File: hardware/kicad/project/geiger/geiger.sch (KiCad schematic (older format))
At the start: 41 parts, among them J1 Pulse Out, J2 I2C OLED 128x64 with SH1106, Q1 BC328, Q2 MPSA44, Q3 BC517, U1 EzSBC_ESP32-01, U2 TLC555xP, U3 TLC555xP

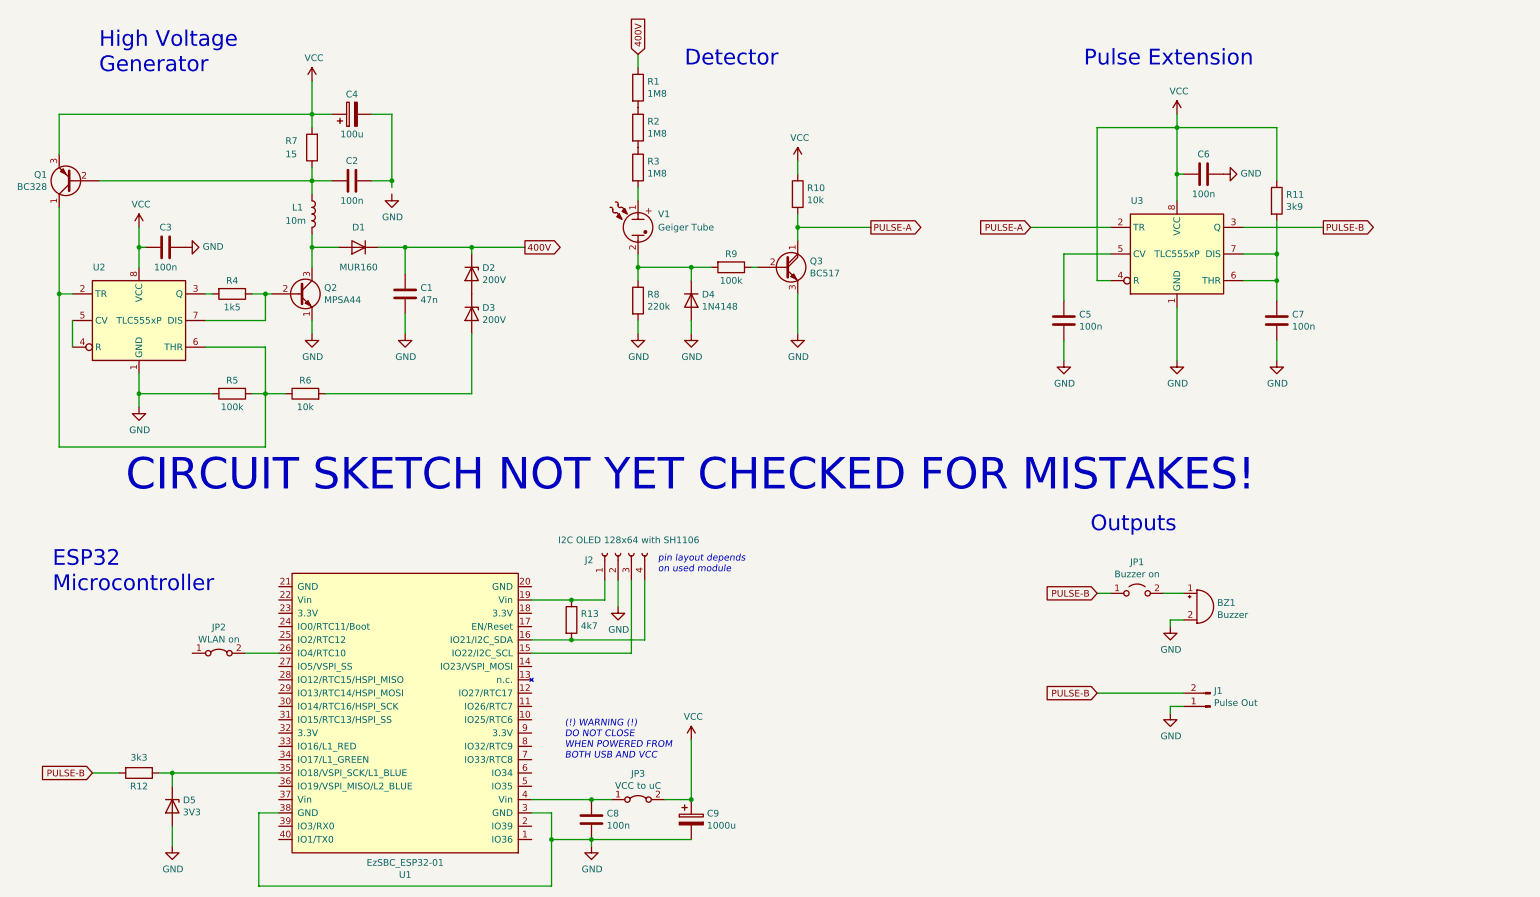
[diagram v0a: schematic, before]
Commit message: checked and corrected KiCad schematic
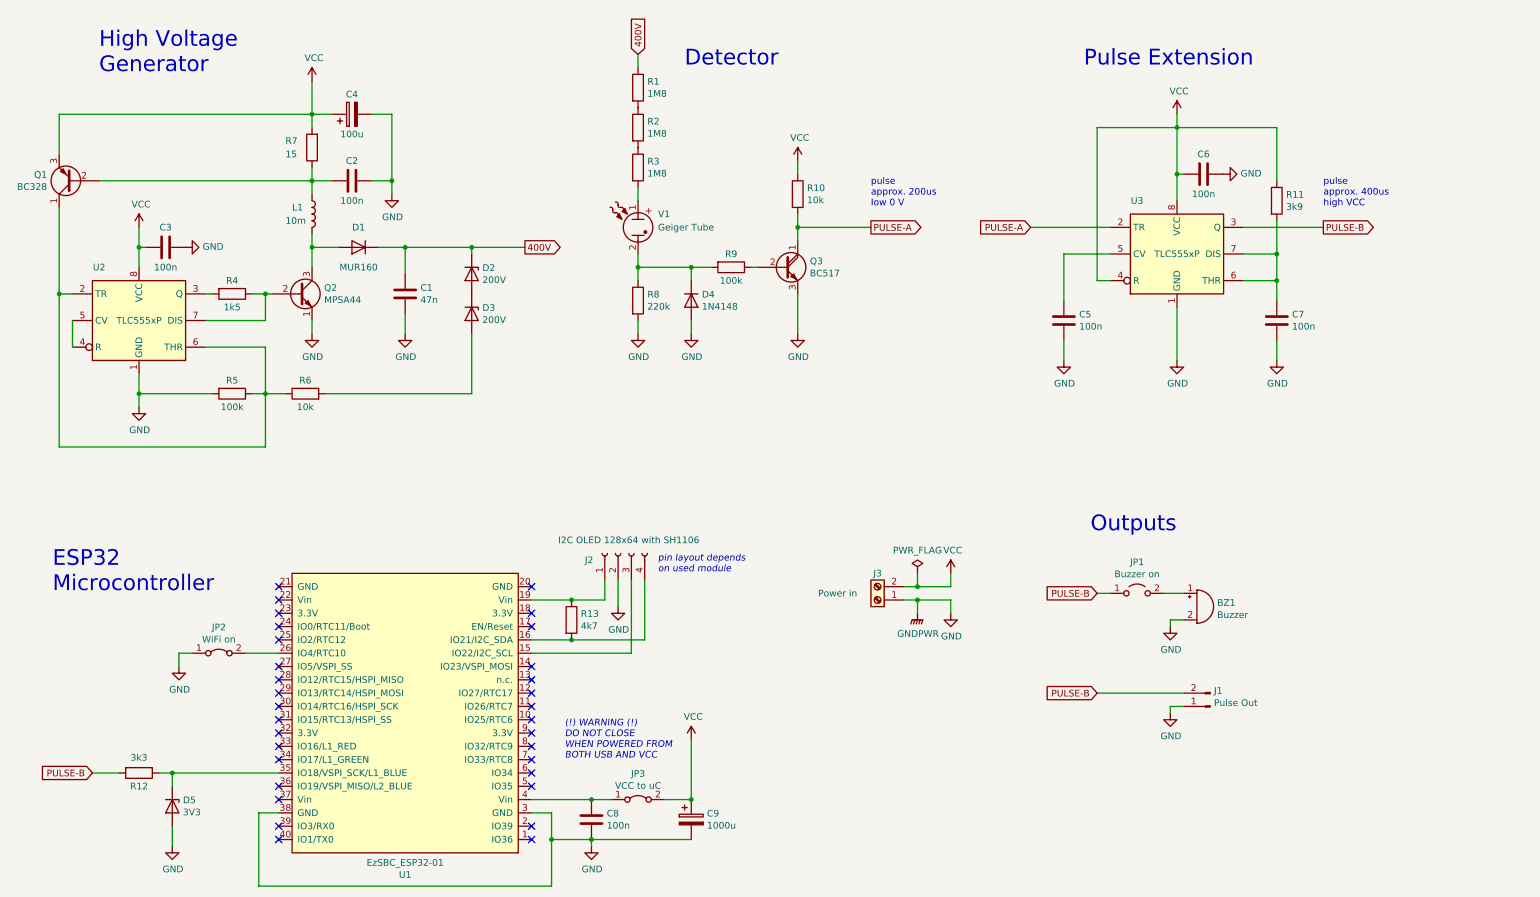
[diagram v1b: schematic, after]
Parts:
- added J3: Power in, symbol Connector:Screw_Terminal_01x02
- JP2: value WLAN on -> WiFi on
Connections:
- net GND: now also C2.1, C4.2, JP2.1 (A), J3.1 (Pin_1)
- net VCC: now also J3.2 (Pin_2)
- no-connect marks 0 -> 32
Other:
- note added: "pulse\napprox. 200us\nlow 0 V"
- note added: "pulse\napprox. 400us\nhigh VCC"
- note removed: "CIRCUIT SKETCH NOT YET CHECKED FOR MISTAKES!"
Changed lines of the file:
@@
 Sheet 1 1
 Title "ESP32 Geiger Counter"
-Date "2021-01-29"
+Date "2021-01-30"
 Rev ""
 Comp "Holger Fleischmann"
@@
 	2950 1750 2950 1650
 Wire Wire Line
-	2950 1650 1050 1650
-Wire Wire Line
 	1050 1650 1050 1950
 Wire Wire Line
@@
 	3100 1650 2950 1650
 Wire Wire Line
-	3550 2150 3550 2200
-Wire Wire Line
 	3400 2150 3550 2150
 Wire Wire Line
@@
 Wire Wire Line
 	2700 5700 2450 5700
-$Comp
-L Jumper:Jumper_2_Bridged JP2
-U 1 1 60343981
-P 2250 5700
-F 0 "JP2" H 2250 5895 50  0000 C CNN
-F 1 "WLAN on" H 2250 5804 50  0000 C CNN
-F 2 "" H 2250 5700 50  0001 C CNN
-F 3 "~" H 2250 5700 50  0001 C CNN
-	1    2250 5700
-	1    0    0    -1
-$EndComp
 Wire Wire Line
 	5050 6800 5200 6800
@@
 Wire Wire Line
 	4900 5600 5450 5600
-Text Notes 1550 4500 0    236  ~ 0
-CIRCUIT SKETCH NOT YET CHECKED FOR MISTAKES!
+Text Notes 7150 2350 0    50   ~ 0
+pulse\napprox. 200us\nlow 0 V
+Text Notes 10550 2350 0    50   ~ 0
+pulse\napprox. 400us\nhigh VCC
+Wire Wire Line
+	3550 2150 3550 2250
+NoConn ~ 2700 5200
+NoConn ~ 2700 5300
+NoConn ~ 2700 5400
+NoConn ~ 2700 5500
+NoConn ~ 2700 5600
+NoConn ~ 2700 5800
+NoConn ~ 2700 5900
+NoConn ~ 2700 6000
+NoConn ~ 2700 6100
+NoConn ~ 2700 6200
+NoConn ~ 2700 6300
+NoConn ~ 2700 6400
+NoConn ~ 2700 6500
+NoConn ~ 2700 6700
+NoConn ~ 2700 6800
+NoConn ~ 4600 5200
+NoConn ~ 4600 5400
+NoConn ~ 4600 5500
+NoConn ~ 4600 5800
+NoConn ~ 4600 5900
+NoConn ~ 4600 6000
+NoConn ~ 4600 6100
+NoConn ~ 4600 6200
+NoConn ~ 4600 6300
+NoConn ~ 4600 6400
+NoConn ~ 4600 6500
+NoConn ~ 4600 6600
+NoConn ~ 4600 6700
+NoConn ~ 4600 7000
+NoConn ~ 2700 7000
+NoConn ~ 2700 7100
+NoConn ~ 4600 7100
+$Comp
+L power:GND #PWR0101
+U 1 1 601D64A6
+P 1950 5800
+F 0 "#PWR0101" H 1950 5550 50  0001 C CNN
+F 1 "GND" H 1955 5627 50  0000 C CNN
+F 2 "" H 1950 5800 50  0001 C CNN
+F 3 "" H 1950 5800 50  0001 C CNN
+	1    1950 5800
+	1    0    0    -1
+$EndComp
+Wire Wire Line
+	2050 5700 1950 5700
+Wire Wire Line
+	1950 5700 1950 5800
+$Comp
+L Jumper:Jumper_2_Bridged JP2
+U 1 1 60343981
+P 2250 5700
+F 0 "JP2" H 2250 5895 50  0000 C CNN
+F 1 "WiFi on" H 2250 5804 50  0000 C CNN
+F 2 "" H 2250 5700 50  0001 C CNN
+F 3 "~" H 2250 5700 50  0001 C CNN
+	1    2250 5700
+	1    0    0    -1
+$EndComp
+Wire Wire Line
+	1050 1650 2950 1650
+$Comp
+L power:GND #PWR024
+U 1 1 601E1EB9
+P 7750 5400
+F 0 "#PWR024" H 7750 5150 50  0001 C CNN
+F 1 "GND" H 7755 5227 50  0000 C CNN
+F 2 "" H 7750 5400 50  0001 C CNN
+F 3 "" H 7750 5400 50  0001 C CNN
+	1    7750 5400
+	1    0    0    -1
+$EndComp
+$Comp
+L power:VCC #PWR023
+U 1 1 601E23DB
+P 7750 5100
+F 0 "#PWR023" H 7750 4950 50  0001 C CNN
+F 1 "VCC" H 7765 5273 50  0000 C CNN
+F 2 "" H 7750 5100 50  0001 C CNN
+F 3 "" H 7750 5100 50  0001 C CNN
+	1    7750 5100
+	1    0    0    -1
+$EndComp
+$Comp
+L Connector:Screw_Terminal_01x02 J3
+U 1 1 601E2CC3
+P 7200 5300
+F 0 "J3" H 7200 5100 50  0000 C CNN
+F 1 "Power in" H 7500 5250 50  0000 C CNN
+F 2 "" H 7200 5300 50  0001 C CNN
+F 3 "~" H 7200 5300 50  0001 C CNN
+	1    7200 5300
+	-1   0    0    1
+$EndComp
+Wire Wire Line
+	7400 5300 7500 5300
+$Comp
+L power:GNDPWR #PWR0102
+U 1 1 601FD717
+P 7500 5400
+F 0 "#PWR0102" H 7500 5200 50  0001 C CNN
+F 1 "GNDPWR" H 7504 5246 50  0000 C CNN
+F 2 "" H 7500 5350 50  0001 C CNN
+F 3 "" H 7500 5350 50  0001 C CNN
+	1    7500 5400
+	1    0    0    -1
+$EndComp
+$Comp
+L power:PWR_FLAG #FLG0101
+U 1 1 601FEC15
+P 7500 5100
+F 0 "#FLG0101" H 7500 5175 50  0001 C CNN
+F 1 "PWR_FLAG" H 7500 5273 50  0000 C CNN
+F 2 "" H 7500 5100 50  0001 C CNN
+F 3 "~" H 7500 5100 50  0001 C CNN
+	1    7500 5100
+	1    0    0    -1
+$EndComp
+Wire Wire Line
+	7500 5400 7500 5300
+Connection ~ 7500 5300
+Wire Wire Line
+	7400 5200 7500 5200
+Wire Wire Line
+	7500 5100 7500 5200
+Connection ~ 7500 5200
+Wire Wire Line
+	7750 5200 7750 5100
+Wire Wire Line
+	7500 5200 7750 5200
+Wire Wire Line
+	7750 5300 7750 5400
+Wire Wire Line
+	7500 5300 7750 5300
 $EndSCHEMATC

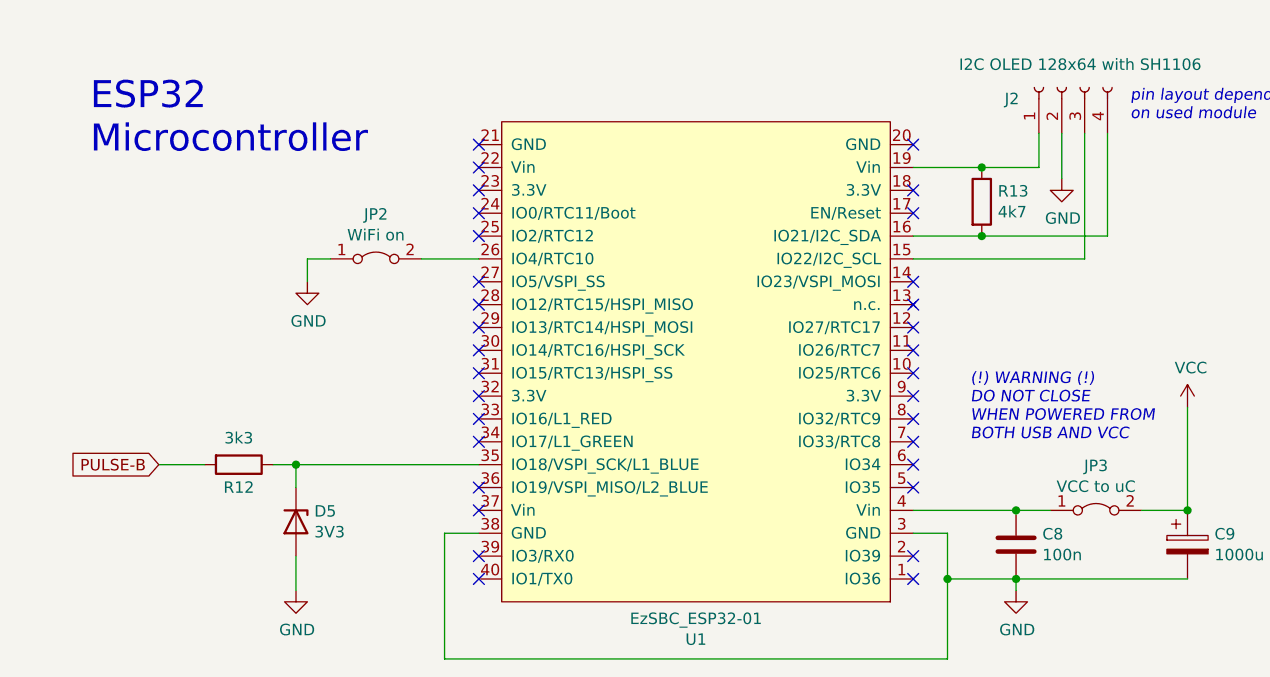
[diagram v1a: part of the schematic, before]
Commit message: changed pins for EZSCB ESP32
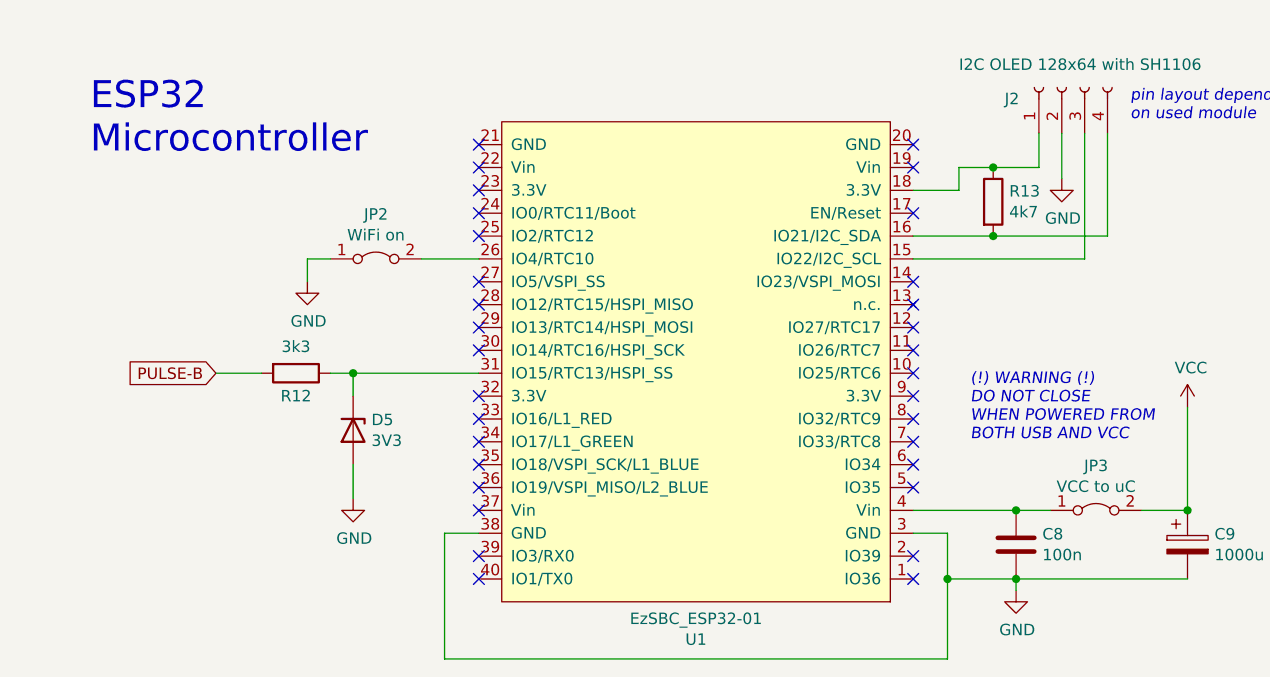
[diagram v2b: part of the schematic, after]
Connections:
- net at D5.1 (K), R12.1: now also U1.31 (IO15/RTC13/HSPI_SS); no longer U1.35 (IO18/VSPI_SCK/L1_BLUE)
- net at U1.18 (3.3V): now also J2.1 (Pin_1), R13.1
- now unconnected: U1.19 (Vin)
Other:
- moved on the sheet: D5, R12, R13
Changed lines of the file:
@@
 Sheet 1 1
 Title "ESP32 Geiger Counter"
-Date "2021-01-30"
+Date "2021-03-07"
 Rev ""
 Comp "Holger Fleischmann"
@@
 L Device:R R12
 U 1 1 602C68B9
-P 1650 6600
-F 0 "R12" V 1750 6600 50  0000 C CNN
-F 1 "3k3" V 1534 6600 50  0000 C CNN
-F 2 "" V 1580 6600 50  0001 C CNN
-F 3 "~" H 1650 6600 50  0001 C CNN
-	1    1650 6600
+P 1900 6200
+F 0 "R12" V 2000 6200 50  0000 C CNN
+F 1 "3k3" V 1784 6200 50  0000 C CNN
+F 2 "" V 1830 6200 50  0001 C CNN
+F 3 "~" H 1900 6200 50  0001 C CNN
+	1    1900 6200
 	0    1    1    0
 $EndComp
@@
 L Device:D_Zener D5
 U 1 1 602C754E
-P 1900 6850
-F 0 "D5" V 1854 6930 50  0000 L CNN
-F 1 "3V3" V 1945 6930 50  0000 L CNN
-F 2 "" H 1900 6850 50  0001 C CNN
-F 3 "~" H 1900 6850 50  0001 C CNN
-	1    1900 6850
+P 2150 6450
+F 0 "D5" V 2104 6530 50  0000 L CNN
+F 1 "3V3" V 2195 6530 50  0000 L CNN
+F 2 "" H 2150 6450 50  0001 C CNN
+F 3 "~" H 2150 6450 50  0001 C CNN
+	1    2150 6450
 	0    1    1    0
 $EndComp
-Text GLabel 1300 6600 0    50   Input ~ 0
+Text GLabel 1550 6200 0    50   Input ~ 0
 PULSE-B
 Wire Wire Line
-	1300 6600 1500 6600
+	1550 6200 1750 6200
 $Comp
 L power:GND #PWR017
 U 1 1 602CD14A
-P 1900 7150
-F 0 "#PWR017" H 1900 6900 50  0001 C CNN
-F 1 "GND" H 1905 6977 50  0000 C CNN
-F 2 "" H 1900 7150 50  0001 C CNN
-F 3 "" H 1900 7150 50  0001 C CNN
-	1    1900 7150
+P 2150 6750
+F 0 "#PWR017" H 2150 6500 50  0001 C CNN
+F 1 "GND" H 2155 6577 50  0000 C CNN
+F 2 "" H 2150 6750 50  0001 C CNN
+F 3 "" H 2150 6750 50  0001 C CNN
+	1    2150 6750
 	1    0    0    -1
 $EndComp
@@
 $EndComp
 Wire Wire Line
-	1800 6600 1900 6600
-Connection ~ 1900 6600
-Wire Wire Line
-	1900 6600 2700 6600
-Wire Wire Line
-	1900 6600 1900 6700
-Wire Wire Line
-	1900 7000 1900 7150
+	2050 6200 2150 6200
+Wire Wire Line
+	2150 6200 2150 6300
+Wire Wire Line
+	2150 6600 2150 6750
 $Comp
 L Device:C C8
@@
 L Device:R R13
 U 1 1 603B2486
-P 4900 5450
-F 0 "R13" H 4970 5496 50  0000 L CNN
-F 1 "4k7" H 4970 5405 50  0000 L CNN
-F 2 "" V 4830 5450 50  0001 C CNN
-F 3 "~" H 4900 5450 50  0001 C CNN
-	1    4900 5450
-	1    0    0    -1
-$EndComp
-Wire Wire Line
-	4600 5600 4900 5600
-Wire Wire Line
-	4600 5300 4900 5300
-Connection ~ 4900 5300
-Wire Wire Line
-	4900 5300 5150 5300
-Connection ~ 4900 5600
-Wire Wire Line
-	4900 5600 5450 5600
+P 4950 5450
+F 0 "R13" H 5020 5496 50  0000 L CNN
+F 1 "4k7" H 5020 5405 50  0000 L CNN
+F 2 "" V 4880 5450 50  0001 C CNN
+F 3 "~" H 4950 5450 50  0001 C CNN
+	1    4950 5450
+	1    0    0    -1
+$EndComp
+Wire Wire Line
+	4600 5600 4950 5600
+Wire Wire Line
+	4950 5300 5150 5300
+Connection ~ 4950 5600
+Wire Wire Line
+	4950 5600 5450 5600
 Text Notes 7150 2350 0    50   ~ 0
 pulse\napprox. 200us\nlow 0 V
@@
 NoConn ~ 2700 6000
 NoConn ~ 2700 6100
-NoConn ~ 2700 6200
 NoConn ~ 2700 6300
 NoConn ~ 2700 6400
@@
 NoConn ~ 2700 6800
 NoConn ~ 4600 5200
-NoConn ~ 4600 5400
 NoConn ~ 4600 5500
 NoConn ~ 4600 5800
@@
 Wire Wire Line
 	7500 5300 7750 5300
+Wire Wire Line
+	4800 5400 4600 5400
+Wire Wire Line
+	4800 5300 4800 5400
+Wire Wire Line
+	4950 5300 4800 5300
+Connection ~ 4950 5300
+NoConn ~ 4600 5300
+Wire Wire Line
+	2150 6200 2700 6200
+Connection ~ 2150 6200
+NoConn ~ 2700 6600
 $EndSCHEMATC
